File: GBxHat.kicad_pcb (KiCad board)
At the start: 2 copper layers, 65 x 30 mm, 26 parts, among them IC1 ATMEGA8515L-8AU, J0 Pi Zero, J1 AVR_SPI_6, U1 TXB0108PWR, U2 NLAS4157, X1 8MHz

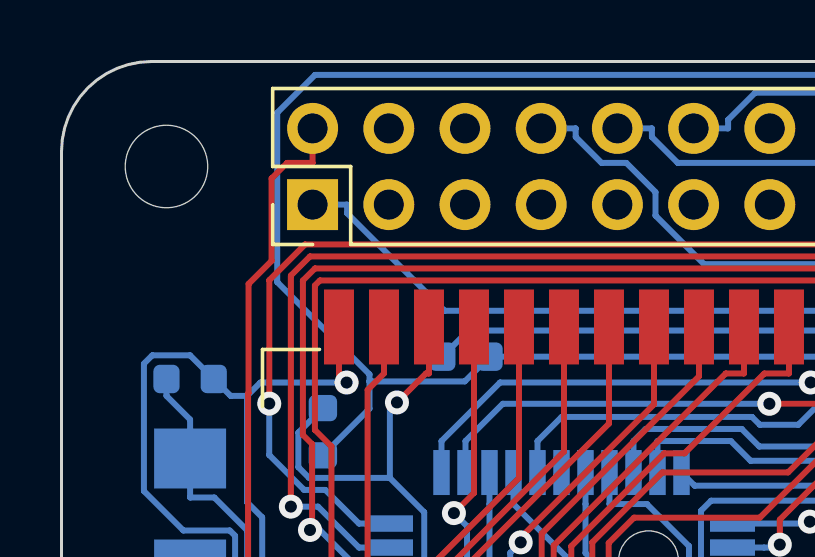
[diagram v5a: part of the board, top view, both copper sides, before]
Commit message: Fix grounding issue and schematic issue
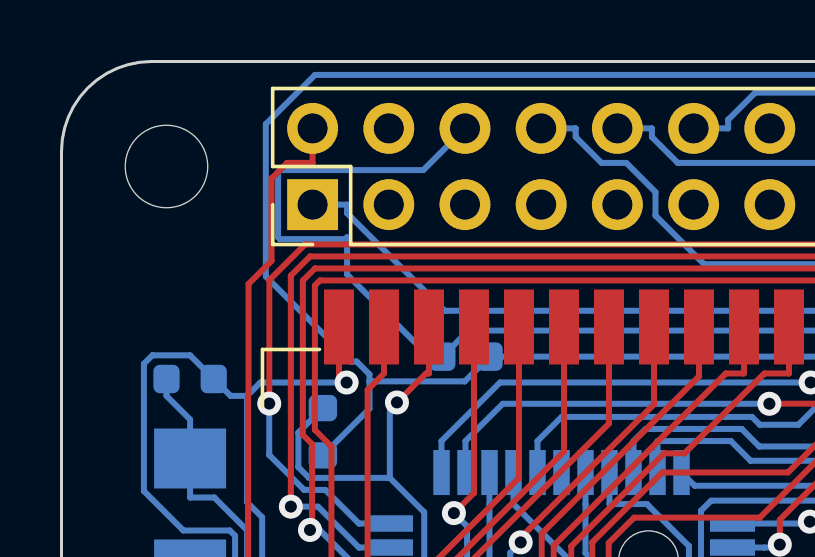
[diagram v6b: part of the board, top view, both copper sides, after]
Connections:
- J0 pad 6: Net-(J0-Pad6) -> GND
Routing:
- net GND: track 188.1 -> 205.0 mm
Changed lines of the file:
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@@
     (thickness 1.6)
     (drawings 10)
-    (tracks 728)
+    (tracks 741)
     (zones 0)
     (modules 26)
-    (nets 92)
+    (nets 91)
   )
   (page A4)
@@
   (net 84 /PI_RX_IN)
   (net 85 /PI_TX_IN)
-  (net 86 "Net-(J0-Pad6)")
-  (net 87 "Net-(U1-Pad13)")
-  (net 88 "Net-(U1-Pad12)")
-  (net 89 "Net-(U1-Pad9)")
-  (net 90 "Net-(U1-Pad8)")
-  (net 91 "Net-(J0-Pad4)")
+  (net 86 "Net-(U1-Pad13)")
+  (net 87 "Net-(U1-Pad12)")
+  (net 88 "Net-(U1-Pad9)")
+  (net 89 "Net-(U1-Pad8)")
+  (net 90 "Net-(J0-Pad4)")
   (net_class Default "This is the default net class."
     (clearance 0.2)
@@
     (add_net "Net-(J0-Pad40)")
     (add_net "Net-(J0-Pad5)")
-    (add_net "Net-(J0-Pad6)")
     (add_net "Net-(J0-Pad7)")
     (add_net "Net-(J0-Pad9)")
@@
       (net 42 /RESET))
     (pad 13 smd rect (at 2.95 -1.625 180) (size 1.45 0.45) (layers B.Cu B.Paste B.Mask)
-      (net 87 "Net-(U1-Pad13)"))
+      (net 86 "Net-(U1-Pad13)"))
     (pad 12 smd rect (at 2.95 -2.275 180) (size 1.45 0.45) (layers B.Cu B.Paste B.Mask)
-      (net 88 "Net-(U1-Pad12)"))
+      (net 87 "Net-(U1-Pad12)"))
     (pad 11 smd rect (at 2.95 -2.925 180) (size 1.45 0.45) (layers B.Cu B.Paste B.Mask)
       (net 1 GND))
@@
       (net 1 GND))
     (pad 9 smd rect (at -2.95 -2.275 180) (size 1.45 0.45) (layers B.Cu B.Paste B.Mask)
-      (net 89 "Net-(U1-Pad9)"))
+      (net 88 "Net-(U1-Pad9)"))
     (pad 8 smd rect (at -2.95 -1.625 180) (size 1.45 0.45) (layers B.Cu B.Paste B.Mask)
-      (net 90 "Net-(U1-Pad8)"))
+      (net 89 "Net-(U1-Pad8)"))
     (pad 7 smd rect (at -2.95 -0.975 180) (size 1.45 0.45) (layers B.Cu B.Paste B.Mask)
       (net 80 /PI_RESET))
@@
       (net 54 "Net-(J0-Pad7)"))
     (pad 6 thru_hole oval (at 2.54 5.08 90) (size 1.7 1.7) (drill 1) (layers *.Cu *.Mask)
-      (net 86 "Net-(J0-Pad6)"))
+      (net 1 GND))
     (pad 5 thru_hole oval (at 0 5.08 90) (size 1.7 1.7) (drill 1) (layers *.Cu *.Mask)
       (net 55 "Net-(J0-Pad5)"))
     (pad 4 thru_hole oval (at 2.54 2.54 90) (size 1.7 1.7) (drill 1) (layers *.Cu *.Mask)
-      (net 91 "Net-(J0-Pad4)"))
+      (net 90 "Net-(J0-Pad4)"))
     (pad 3 thru_hole oval (at 0 2.54 90) (size 1.7 1.7) (drill 1) (layers *.Cu *.Mask)
       (net 56 "Net-(J0-Pad3)"))
@@
   (via (at 209.7677 77.9521) (size 0.8) (layers F.Cu B.Cu) (net 1))
   (via (at 218.0372 90.9956) (size 0.8) (layers F.Cu B.Cu) (net 1))
+  (segment (start 212.324001 70.870699) (end 212.864001 70.330699) (width 0.2) (layer B.Cu) (net 1))
+  (segment (start 207.483999 70.930699) (end 207.543999 70.870699) (width 0.2) (layer B.Cu) (net 1))
+  (segment (start 207.543999 70.870699) (end 212.324001 70.870699) (width 0.2) (layer B.Cu) (net 1))
+  (segment (start 207.483999 73.110701) (end 207.483999 70.930699) (width 0.2) (layer B.Cu) (net 1))
+  (segment (start 209.724001 73.170701) (end 207.543999 73.170701) (width 0.2) (layer B.Cu) (net 1))
+  (segment (start 207.543999 73.170701) (end 207.483999 73.110701) (width 0.2) (layer B.Cu) (net 1))
+  (segment (start 209.784001 73.110701) (end 209.724001 73.170701) (width 0.2) (layer B.Cu) (net 1))
+  (segment (start 212.864001 70.330699) (end 213.714 69.4807) (width 0.2) (layer B.Cu) (net 1))
+  (segment (start 212.521 77.089) (end 209.784001 74.352001) (width 0.2) (layer B.Cu) (net 1))
+  (segment (start 209.784001 74.352001) (end 209.784001 73.110701) (width 0.2) (layer B.Cu) (net 1))
+  (segment (start 212.9585 77.089) (end 212.521 77.089) (width 0.2) (layer B.Cu) (net 1))
   (segment (start 219.331 92.3521) (end 219.331 93.4024) (width 0.2) (layer B.Cu) (net 2))
   (segment (start 203.7635 86.8341) (end 211.1365 94.2071) (width 0.2) (layer B.Cu) (net 2))
@@
   (segment (start 256.014 76.0997) (end 256.014 74.6497) (width 0.2) (layer F.Cu) (net 5))
   (segment (start 256.014 74.6497) (end 255.651 74.2867) (width 0.2) (layer F.Cu) (net 5))
-  (segment (start 208.715297 67.697401) (end 207.4545 68.958198) (width 0.2) (layer B.Cu) (net 5))
+  (segment (start 209.911219 77.252099) (end 210.103701 77.252099) (width 0.2) (layer B.Cu) (net 5))
+  (segment (start 210.103701 77.252099) (end 210.5307 77.679098) (width 0.2) (layer B.Cu) (net 5))
   (segment (start 255.651 68.0974) (end 255.251001 67.697401) (width 0.2) (layer B.Cu) (net 5))
   (segment (start 255.251001 67.697401) (end 208.715297 67.697401) (width 0.2) (layer B.Cu) (net 5))
+  (segment (start 208.715297 67.697401) (end 207.07604 69.336658) (width 0.2) (layer B.Cu) (net 5))
+  (segment (start 207.07604 69.336658) (end 207.07604 74.41692) (width 0.2) (layer B.Cu) (net 5))
   (segment (start 210.5307 77.679098) (end 210.5307 77.9143) (width 0.2) (layer B.Cu) (net 5))
-  (segment (start 207.4545 74.602898) (end 210.5307 77.679098) (width 0.2) (layer B.Cu) (net 5))
-  (segment (start 207.4545 68.958198) (end 207.4545 74.602898) (width 0.2) (layer B.Cu) (net 5))
+  (segment (start 207.07604 74.41692) (end 209.911219 77.252099) (width 0.2) (layer B.Cu) (net 5))
   (segment (start 242.514 77.65) (end 239.702 80.462) (width 0.2) (layer F.Cu) (net 6))
   (segment (start 239.702 80.462) (end 229.9769 80.462) (width 0.2) (layer F.Cu) (net 6))
@@
   (segment (start 263.38986 83.0382) (end 262.910429 83.517631) (width 0.2) (layer F.Cu) (net 58))
   (segment (start 264.252 83.0382) (end 263.38986 83.0382) (width 0.2) (layer F.Cu) (net 58))
-  (via (at 262.51043 83.91763) (size 0.8) (drill 0.4) (layers F.Cu B.Cu) (net 58) (status 1000000))
+  (via (at 262.51043 83.91763) (size 0.8) (drill 0.4) (layers F.Cu B.Cu) (net 58))
   (segment (start 261.1935 79.6157) (end 261.93832 80.36052) (width 0.2) (layer B.Cu) (net 59))
   (segment (start 261.1935 79.1407) (end 261.1935 79.6157) (width 0.2) (layer B.Cu) (net 59))
